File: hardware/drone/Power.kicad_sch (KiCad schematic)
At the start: 99 parts, among them Q1 ISP650P06NM, U1 STM32N645I0, U12 LP5907, U16 LMR51635XFDDCR, U18 TPS2121, U3 TPS628303, U4 TPS7A2118PQWDSGRQ1, U5 TPS628303

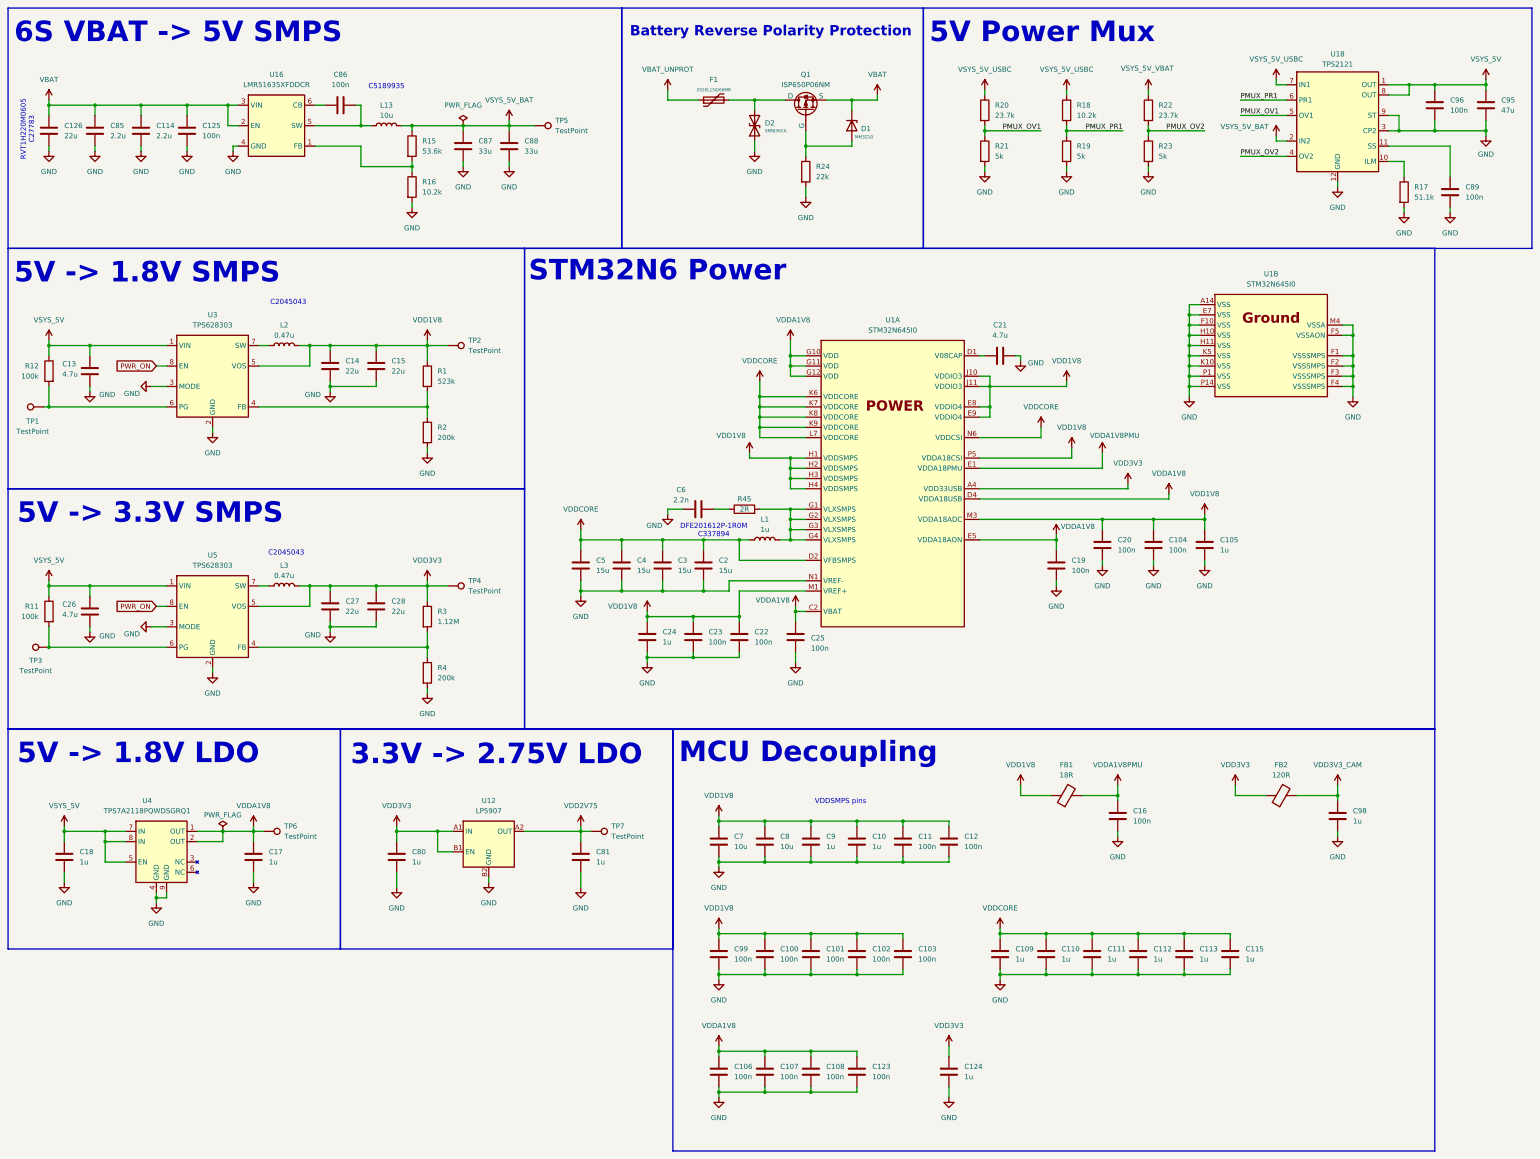
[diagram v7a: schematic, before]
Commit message: Labeled nets, added colours, and fixed stm32n6 schematic symbol issues
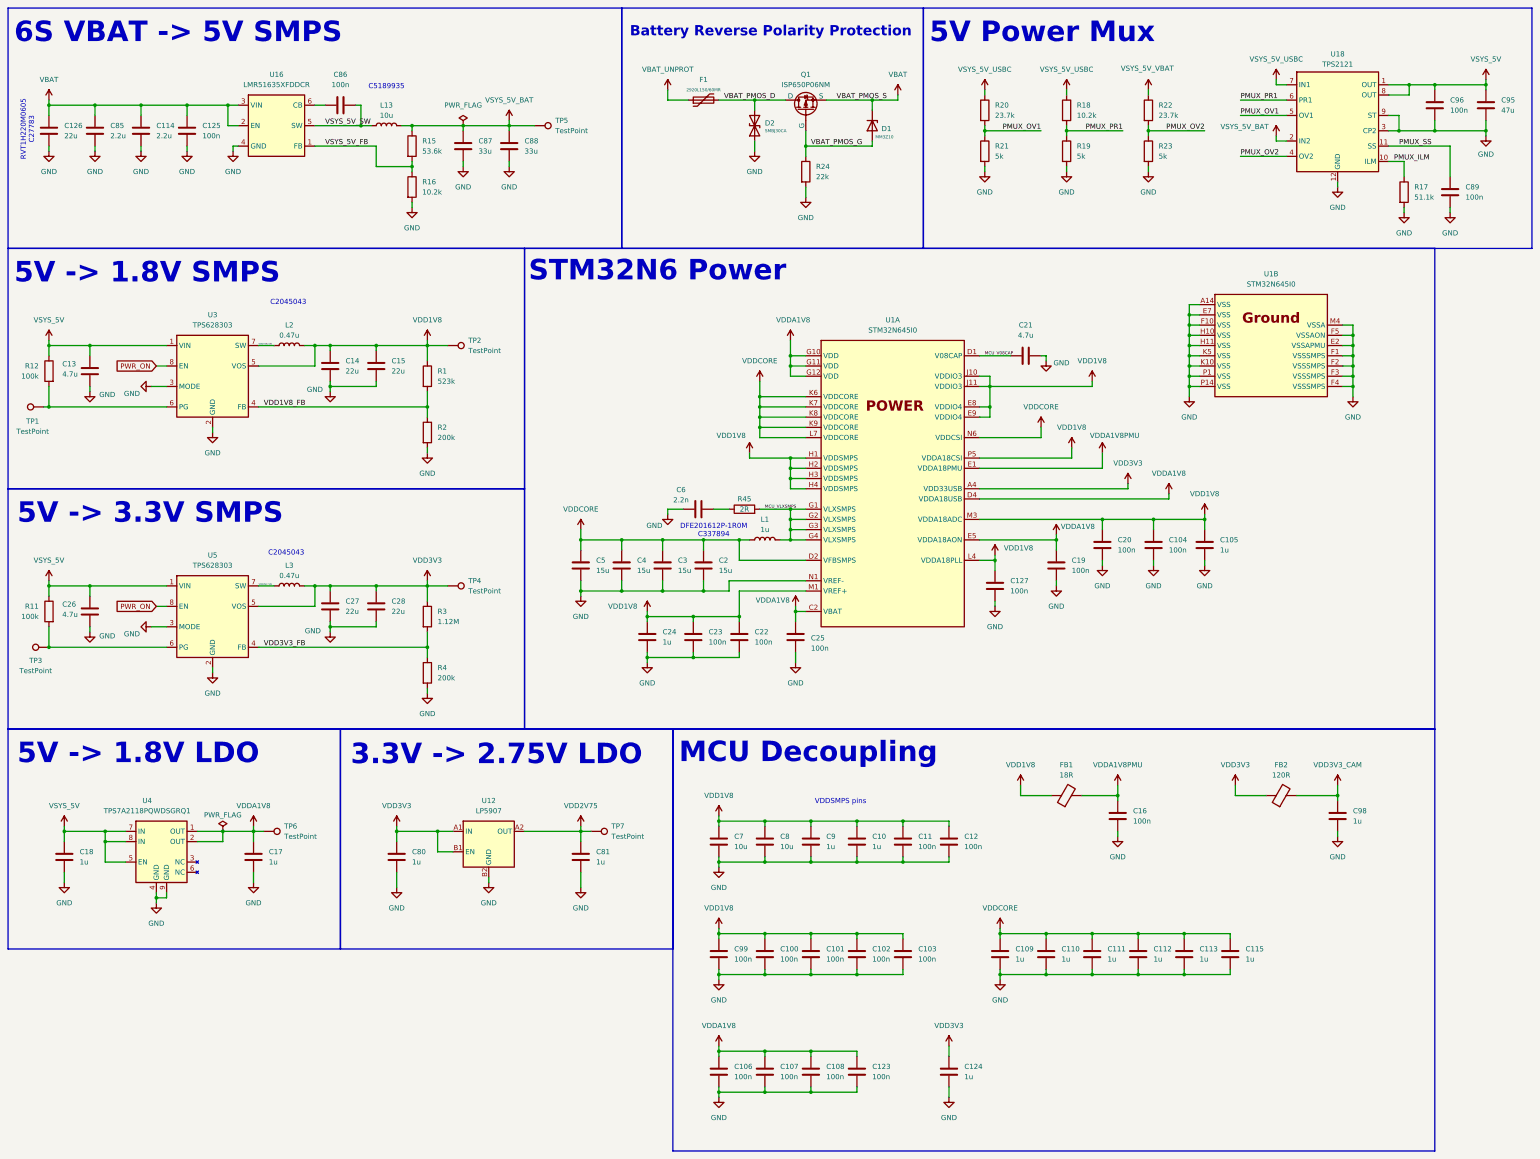
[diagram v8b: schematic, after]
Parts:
- added C127: 100n, Capacitor_SMD:C_0201_0603Metric, symbol Device:C
- U1: footprint STM32N645I0:BGA178C80P14X14_1200X1200X100 -> (none)
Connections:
- net GND: now also U1.E2 (VSSAPMU), C127.2
- net VDD1V8: now also U1.L4 (VDDA18PLL), C127.1
- net PMUX_ILM: now reaches R17.1, U18.10 (ILM)
- net PMUX_SS: now reaches C89.1, U18.11 (SS)
- net VSYS_5V_SW: now reaches C86.2, L13.1, U16.5 (SW)
- net VBAT_PMOS_G: now reaches D1.2 (A), Q1.2 (G), R24.1
- net VSYS_5V_FB: now reaches R15.2, R16.1, U16.1 (FB)
- net MCU_VLXSMPS: now reaches L1.2, R45.2, U1.G1 (VLXSMPS), U1.G2 (VLXSMPS), U1.G3 (VLXSMPS), U1.G4 (VLXSMPS)
- net VDD3V3_FB: now reaches R3.2, R4.1, U5.4 (FB)
- net VDD1V8_FB: now reaches R1.2, R2.1, U3.4 (FB)
- net VDD1V8_SW: now reaches L2.1, U3.7 (SW)
- net MCU_V08CAP: now reaches C21.2, U1.D1 (V08CAP)
- net VBAT_PMOS_D: now reaches D2.2 (A2), F1.2, Q1.1 (D)
- net VDD3V3_SW: now reaches L3.1, U5.7 (SW)
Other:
- moved on the sheet: C21, D1, F1, L2, L3
